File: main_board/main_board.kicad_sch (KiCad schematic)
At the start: 59 parts, among them J1 USB4105-GF-A-060, J2 Conn_ARM_JTAG_SWD_10, Q3 NX3008PBK,215, U1 SSD1306, U2 ESP32-S2-SOLO, U3 TLV62568PDRLT, U4 MCP73832, U7 MAX17055, Y1 SC32S-7PF20PPM

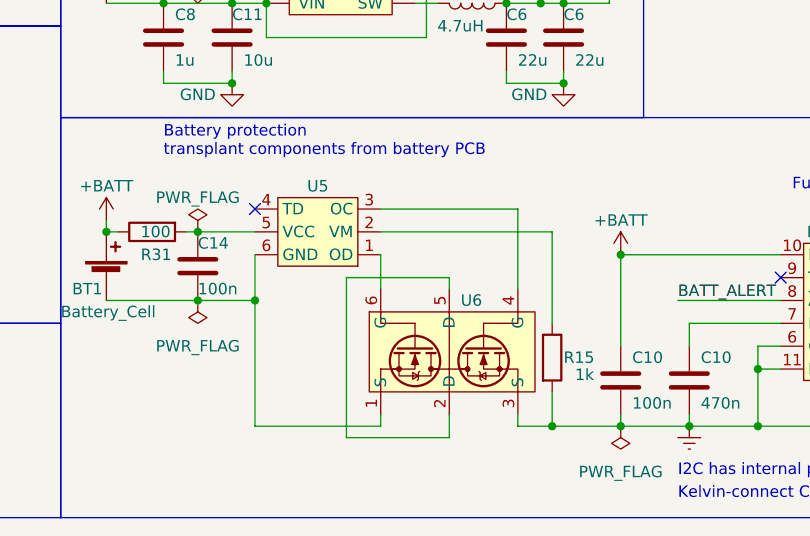
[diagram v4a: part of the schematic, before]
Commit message: Close #32: Add missing silk screen
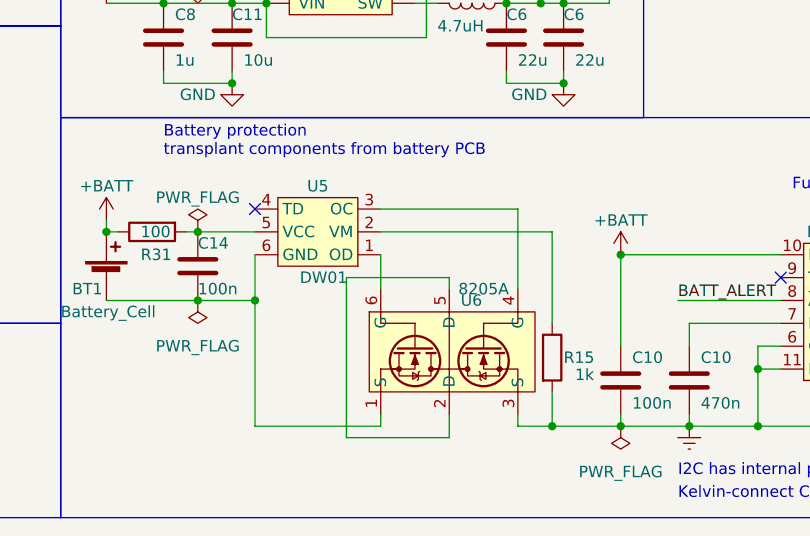
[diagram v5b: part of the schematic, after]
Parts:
- JP1: now left out of the parts list
- U5: value ~ -> DW01
- U6: value ~ -> 8205A
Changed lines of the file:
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@@
   (title_block
     (title "Card/IO ECG main board")
-    (date "2023-08-24")
-    (rev "4")
+    (date "2023-09-08")
+    (rev "5")
   )
   (junction (at 200.66 135.89) (diameter 0) (color 0 0 0 0)
@@
   )
   (symbol (lib_id "Jumper:SolderJumper_3_Open") (at 127 82.55 90) (mirror x) (unit 1)
-    (in_bom yes) (on_board yes) (dnp no)
+    (in_bom no) (on_board yes) (dnp no)
     (property "Reference" "JP1" (at 124.46 81.915 90)
       (effects (font (size 1.27 1.27)) (justify left))
@@
   )
   (symbol (lib_id "main_board_parts:DW01") (at 87.63 165.1 180) (unit 1)
-    (in_bom yes) (on_board yes) (dnp no) (fields_autoplaced)
+    (in_bom yes) (on_board yes) (dnp no)
     (property "Reference" "U5" (at 88.265 160.02 0)
       (effects (font (size 1.27 1.27)))
     )
-    (property "Value" "~" (at 92.71 165.1 0)
+    (property "Value" "DW01" (at 88.9 170.18 0)
       (effects (font (size 1.27 1.27)))
     )
@@
       (effects (font (size 1.27 1.27)) (justify right))
     )
-    (property "Value" "~" (at 97.79 182.88 0)
-      (effects (font (size 1.27 1.27)))
-    )
+    (property "Value" "8205A" (at 106.68 171.45 90)
+      (effects (font (size 1.27 1.27)))
+    )

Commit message: Close #33: Clean up RLD
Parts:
- removed R16: 1M, Resistor_SMD:R_0603_1608Metric, symbol Device:R
- E1: footprint main_board_parts:SplitElectrode -> main_board_parts:Electrode; symbol main_board_parts:SplitElectrode -> main_board_parts:Electrode
- R17: value 1M -> 2k
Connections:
- net at E1.1: now also M1.1 (ECG_L)
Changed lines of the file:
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@@
   (junction (at 64.77 165.1) (diameter 0) (color 0 0 0 0)
   )
-  (junction (at 60.96 66.04) (diameter 0) (color 0 0 0 0)
-  )
   (junction (at 78.74 139.7) (diameter 0) (color 0 0 0 0)
   )
@@
     (stroke (width 0) (type default))
   )
-  (wire (pts (xy 40.64 67.31) (xy 55.88 67.31))
-    (stroke (width 0) (type default))
-  )
   (wire (pts (xy 177.8 50.8) (xy 177.8 55.88))
     (stroke (width 0) (type default))
@@
     (stroke (width 0) (type default))
   )
-  (wire (pts (xy 60.96 66.04) (xy 60.96 74.93))
+  (wire (pts (xy 60.96 63.5) (xy 60.96 74.93))
     (stroke (width 0) (type default))
   )
@@
     (stroke (width 0) (type default))
   )
-  (wire (pts (xy 55.88 63.5) (xy 55.88 67.31))
+  (wire (pts (xy 55.88 63.5) (xy 55.88 66.04))
     (stroke (width 0) (type default))
   )
@@
     (stroke (width 0) (type default))
   )
-  (wire (pts (xy 40.64 66.04) (xy 46.99 66.04))
+  (wire (pts (xy 40.64 66.04) (xy 55.88 66.04))
     (stroke (width 0) (type default))
   )
@@
     (stroke (width 0) (type default))
   )
-  (wire (pts (xy 60.96 66.04) (xy 60.96 63.5))
-    (stroke (width 0) (type default))
-  )
   (wire (pts (xy 71.12 139.7) (xy 78.74 139.7))
     (stroke (width 0) (type default))
@@
     (stroke (width 0) (type default))
   )
-  (wire (pts (xy 54.61 66.04) (xy 60.96 66.04))
-    (stroke (width 0) (type default))
-  )
   (wire (pts (xy 240.03 135.89) (xy 240.03 139.7))
     (stroke (width 0) (type default))
@@
     )
   )
-  (symbol (lib_id "main_board_parts:SplitElectrode") (at 38.1 66.04 0) (mirror y) (unit 1)
+  (symbol (lib_id "main_board_parts:Electrode") (at 38.1 66.04 0) (mirror y) (unit 1)
     (in_bom no) (on_board yes) (dnp no) (fields_autoplaced)
     (property "Reference" "E1" (at 35.56 62.23 0)
@@
       (effects (font (size 1.27 1.27)))
     )
-    (property "Footprint" "main_board_parts:SplitElectrode" (at 37.973 69.85 0)
+    (property "Footprint" "main_board_parts:Electrode" (at 38.1 66.04 0)
       (effects (font (size 1.27 1.27)) hide)
     )
@@
     )
     (pin "1")
-    (pin "2")
     (instances
       (project "main_board"
@@
       (effects (font (size 1.27 1.27)) (justify left))
     )
-    (property "Value" "1M" (at 49.53 74.93 90)
+    (property "Value" "2k" (at 49.53 74.93 90)
       (effects (font (size 1.27 1.27)) (justify left))
     )
@@
         )
       )
-    )
-  )
-  (symbol (lib_id "Device:R") (at 50.8 66.04 270) (mirror x) (unit 1)
-    (in_bom yes) (on_board yes) (dnp no)
-    (property "Reference" "R16" (at 49.53 63.5 90)
-      (effects (font (size 1.27 1.27)) (justify left))
-    )
-    (property "Value" "1M" (at 49.53 66.04 90)
-      (effects (font (size 1.27 1.27)) (justify left))
-    )
-    (property "Footprint" "Resistor_SMD:R_0603_1608Metric" (at 50.8 67.818 90)
-      (effects (font (size 1.27 1.27)) hide)
-    )
-    (property "Datasheet" "~" (at 50.8 66.04 0)
-      (effects (font (size 1.27 1.27)) hide)
-    )
-    (pin "1")
-    (pin "2")
-    (instances
-      (project "main_board"
-        (path "/e55848cd-275a-4b5e-8e68-b5d8d07c8d31"
-          (reference "R16") (unit 1)
-        )
-      )

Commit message: Clean up
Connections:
- net ADC_EN: now also U2.18 (IO10); no longer U2.12 (IO8)
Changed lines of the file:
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@@
   (junction (at 102.87 55.88) (diameter 0) (color 0 0 0 0)
   )
+  (no_connect (at 129.54 63.5))
   (no_connect (at 254 109.22))
   (no_connect (at 138.43 78.74))
@@
   (no_connect (at 161.29 78.74))
   (no_connect (at 170.18 68.58))
-  (no_connect (at 143.51 78.74))
   (no_connect (at 140.97 78.74))
   (no_connect (at 198.12 147.32))
@@
     (stroke (width 0) (type default))
   )
-  (wire (pts (xy 120.65 63.5) (xy 129.54 63.5))
-    (stroke (width 0) (type default))
-  )
   (wire (pts (xy 151.13 78.74) (xy 151.13 92.71))
     (stroke (width 0) (type default))
@@
   )
   (wire (pts (xy 128.27 27.94) (xy 121.92 27.94))
+    (stroke (width 0) (type default))
+  )
+  (wire (pts (xy 143.51 78.74) (xy 143.51 92.71))
     (stroke (width 0) (type default))
   )
@@
     (effects (font (size 1.27 1.27)) (justify left bottom))
   )
-  (label "ADC_EN" (at 120.65 63.5 0) (fields_autoplaced)
-    (effects (font (size 1.27 1.27)) (justify left bottom))
-  )
+  (label "ADC_EN" (at 143.51 92.71 90) (fields_autoplaced)
+    (effects (font (size 1.27 1.27)) (justify left bottom))
+  )

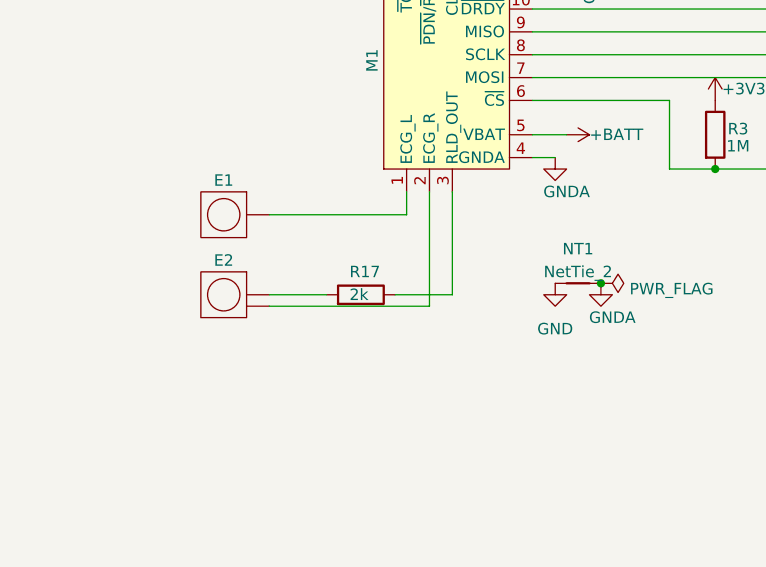
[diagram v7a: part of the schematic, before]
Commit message: Tweak touch detector circuit
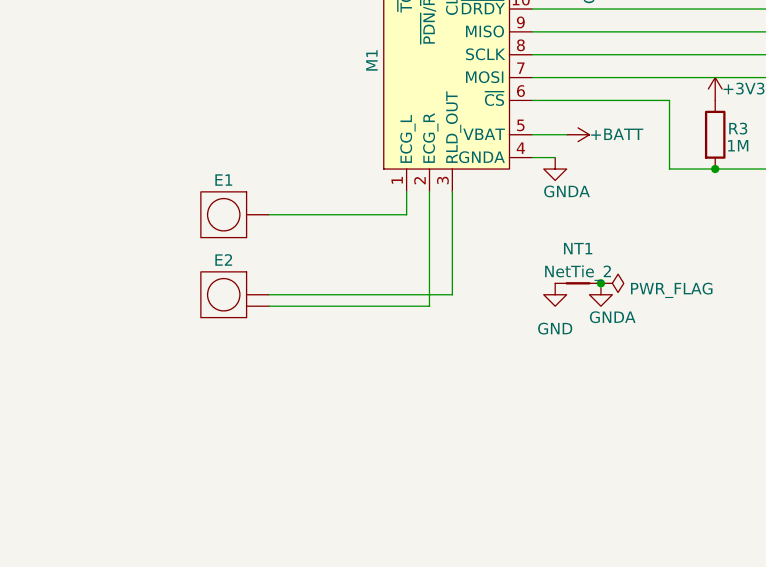
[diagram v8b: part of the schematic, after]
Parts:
- removed R17: 2k, Resistor_SMD:R_0603_1608Metric, symbol Device:R
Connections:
- net at E2.1: now also M1.3 (RLD_OUT)
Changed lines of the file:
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@@
   (title_block
     (title "Card/IO ECG main board")
-    (date "2023-09-08")
+    (date "2023-09-11")
     (rev "5")
   )
@@
     (stroke (width 0) (type default))
   )
-  (wire (pts (xy 60.96 74.93) (xy 54.61 74.93))
-    (stroke (width 0) (type default))
-  )
   (wire (pts (xy 166.37 170.18) (xy 156.21 170.18))
     (stroke (width 0) (type default))
@@
     (stroke (width 0) (type default))
   )
-  (wire (pts (xy 40.64 74.93) (xy 46.99 74.93))
+  (wire (pts (xy 40.64 74.93) (xy 60.96 74.93))
     (stroke (width 0) (type default))
   )
@@
         )
       )
-    )
-  )
-  (symbol (lib_id "Device:R") (at 50.8 74.93 270) (mirror x) (unit 1)
-    (in_bom yes) (on_board yes) (dnp no)
-    (property "Reference" "R17" (at 49.53 72.39 90)
-      (effects (font (size 1.27 1.27)) (justify left))
-    )
-    (property "Value" "2k" (at 49.53 74.93 90)
-      (effects (font (size 1.27 1.27)) (justify left))
-    )
-    (property "Footprint" "Resistor_SMD:R_0603_1608Metric" (at 50.8 76.708 90)
-      (effects (font (size 1.27 1.27)) hide)
-    )
-    (property "Datasheet" "~" (at 50.8 74.93 0)
-      (effects (font (size 1.27 1.27)) hide)
-    )
-    (pin "1")
-    (pin "2")
-    (instances
-      (project "main_board"
-        (path "/e55848cd-275a-4b5e-8e68-b5d8d07c8d31"
-          (reference "R17") (unit 1)
-        )
-      )
